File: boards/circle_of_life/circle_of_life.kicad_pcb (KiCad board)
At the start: 2 copper layers, 87.4 x 96.4 mm, 120 parts, among them IC1 ESP32-WROOM-32E-N8R2, IC2 TC1262-3.3VDB, IC3 TPS565242DRLR, IC4 LT3922EUFD#PBF, IC5 TXU0101DBVR, IC6 CP2102C-A01-GQFN28, J1 Water Pump Connector, J11 LED Connector, J2 Servo Motor Connector, J3 Power Connector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

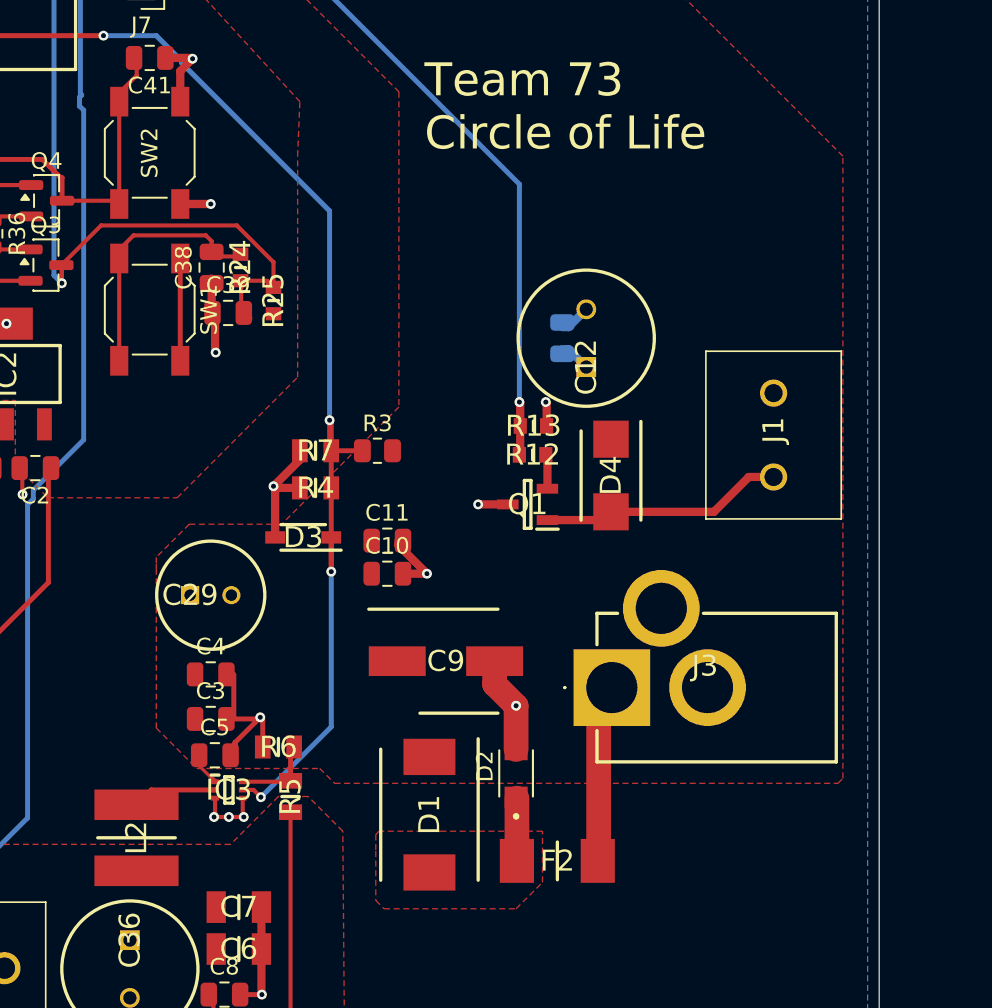
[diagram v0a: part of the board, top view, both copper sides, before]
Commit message: Fixed DRC for main board
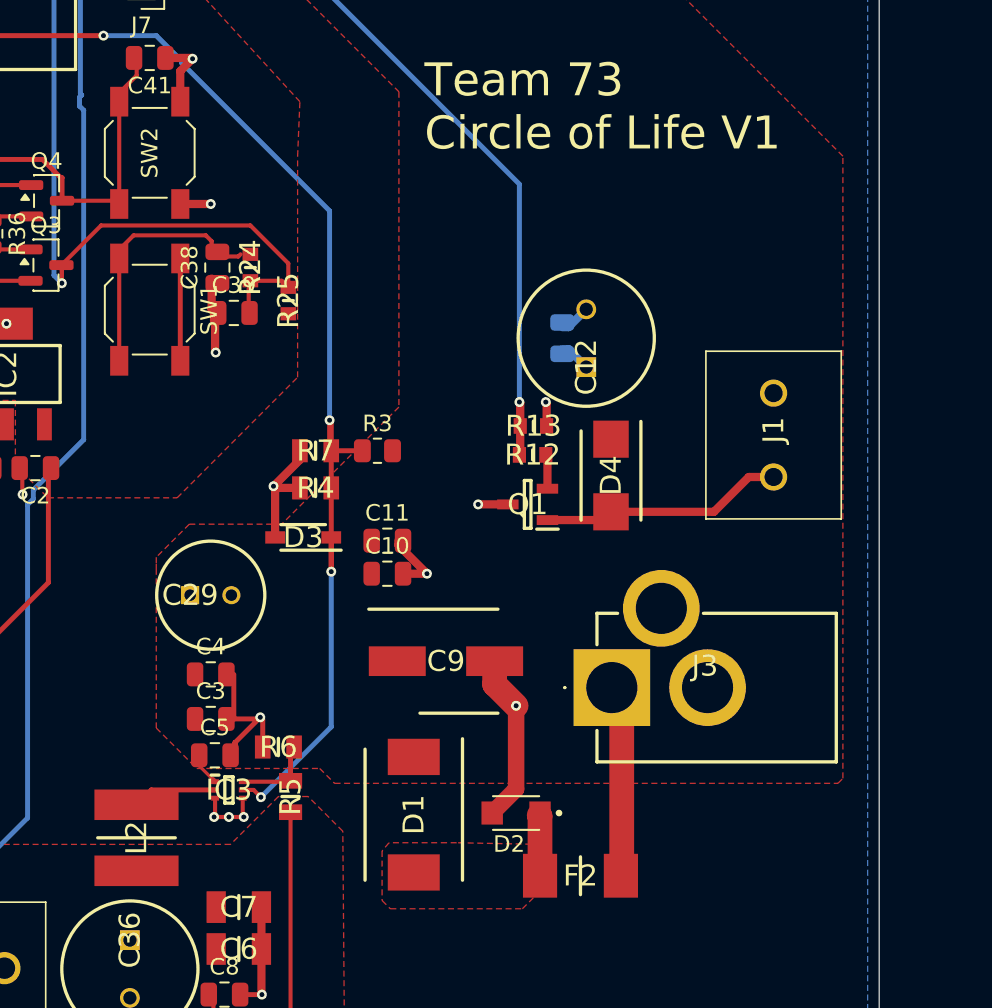
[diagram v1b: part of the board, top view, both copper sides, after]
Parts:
- moved D2 2.40 mm to (151.6, 184.8), turned to 180 degrees
- moved F2 1.66 mm to (155.5, 188.6)
- moved D1 0.95 mm to (145.4, 184.9)
- moved R25 0.90 mm to (137.8, 153.8)
- moved R24 0.60 mm to (135.5, 151.8)
- moved C38 0.35 mm to (133.5, 151.8)
- moved C39 0.35 mm to (134.5, 154.5)
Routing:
- net GND: track 150.0 -> 154.4 mm
- net Net-(D1-A): track 3.87 -> 2.78 mm
- net MCU_EN: track 60.9 -> 61.8 mm
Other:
- board text added: "Team 73 Circle of Life V1"
- board text removed: "Team 73 Circle of Life"
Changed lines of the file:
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@@
 	(footprint "SamacSys_Parts:RESC1608X55N"
 		(layer "F.Cu")
-		(at 134.902935 151.75 -90)
+		(at 135.5 151.75 -90)
 		(descr "RC0603")
 		(tags "Resistor")
@@
 	(footprint "SamacSys_Parts:RESC1608X55N"
 		(layer "F.Cu")
-		(at 136.902935 153.75 -90)
+		(at 137.8 153.75 -90)
 		(descr "RC0603")
 		(tags "Resistor")
@@
 	(footprint "Capacitor_SMD:C_0805_2012Metric"
 		(layer "F.Cu")
-		(at 133.152935 151.75 90)
+		(at 133.5 151.75 90)
 		(descr "Capacitor SMD 0805 (2012 Metric), square (rectangular) end terminal, IPC-7351 nominal, (Body size source: IPC-SM-782 page 76, https://www.pcb-3d.com/wordpress/wp-content/uploads/ipc-sm-782a_amendment_1_and_2.pdf, https://docs.google.com/spreadsheets/d/1BsfQQcO9C6DZCsRaXUlFlo91Tg2WpOkGARC1WS5S8t0/edit?usp=sharing), generated with kicad-footprint-generator")
 		(tags "capacitor")
@@
 	(footprint "Capacitor_SMD:C_0805_2012Metric"
 		(layer "F.Cu")
-		(at 134.152935 154.5)
+		(at 134.5 154.5)
 		(descr "Capacitor SMD 0805 (2012 Metric), square (rectangular) end terminal, IPC-7351 nominal, (Body size source: IPC-SM-782 page 76, https://www.pcb-3d.com/wordpress/wp-content/uploads/ipc-sm-782a_amendment_1_and_2.pdf, https://docs.google.com/spreadsheets/d/1BsfQQcO9C6DZCsRaXUlFlo91Tg2WpOkGARC1WS5S8t0/edit?usp=sharing), generated with kicad-footprint-generator")
 		(tags "capacitor")
@@
 	(footprint "SamacSys_Parts:TVS_SMF12A"
 		(layer "F.Cu")
-		(at 151.6 182.4 90)
+		(at 151.6 184.8 180)
 		(property "Reference" "D2"
-			(at 0.425 -1.885 90)
+			(at 0.425 -1.885 0)
 			(layer "F.SilkS")
 			(effects
@@
 		)
 		(property "Value" "SMF12A"
-			(at -0.25 -2.25 90)
+			(at -0.25 -2.25 0)
 			(layer "F.Fab")
 			(effects
@@
 		)
 		(property "Datasheet" "https://www.vishay.com/doc?85881"
-			(at 0 0 90)
+			(at 0 0 0)
 			(layer "F.Fab")
 			(hide yes)
@@
 		)
 		(property "Description" "200W unidirectional Transil Transient Voltage Suppressor, 12Vrwm, SMF"
-			(at 0 0 90)
+			(at 0 0 0)
 			(layer "F.Fab")
 			(hide yes)
@@
 		(attr smd)
 		(fp_line
-			(start -1.4 -1.02)
-			(end 1.4 -1.02)
+			(start 1.4 1.02)
+			(end -1.4 1.02)
 			(stroke
 				(width 0.127)
@@
 		)
 		(fp_line
-			(start 1.4 1.02)
-			(end -1.4 1.02)
+			(start -1.4 -1.02)
+			(end 1.4 -1.02)
 			(stroke
 				(width 0.127)
@@
 		)
 		(fp_line
-			(start 2.35 -1.125)
-			(end 2.35 1.125)
+			(start 2.35 1.125)
+			(end -2.35 1.125)
 			(stroke
 				(width 0.05)
@@
 		)
 		(fp_line
-			(start -2.35 -1.125)
-			(end 2.35 -1.125)
+			(start 2.35 -1.125)
+			(end 2.35 1.125)
 			(stroke
 				(width 0.05)
@@
 		)
 		(fp_line
-			(start 2.35 1.125)
-			(end -2.35 1.125)
+			(start -2.35 1.125)
+			(end -2.35 -1.125)
 			(stroke
 				(width 0.05)
@@
 		)
 		(fp_line
-			(start -2.35 1.125)
-			(end -2.35 -1.125)
+			(start -2.35 -1.125)
+			(end 2.35 -1.125)
 			(stroke
 				(width 0.05)
@@
 		)
 		(fp_line
-			(start 1.4 -0.875)
-			(end 1.4 0.875)
+			(start 1.4 0.875)
+			(end -1.4 0.875)
 			(stroke
 				(width 0.127)
@@
 		)
 		(fp_line
-			(start -1.4 -0.875)
-			(end 1.4 -0.875)
+			(start 1.4 -0.875)
+			(end 1.4 0.875)
 			(stroke
 				(width 0.127)
@@
 		)
 		(fp_line
-			(start 1.4 0.875)
-			(end -1.4 0.875)
+			(start -1.4 0.875)
+			(end -1.4 -0.875)
 			(stroke
 				(width 0.127)
@@
 		)
 		(fp_line
-			(start -1.4 0.875)
-			(end -1.4 -0.875)
+			(start -1.4 -0.875)
+			(end 1.4 -0.875)
 			(stroke
 				(width 0.127)
@@
 		)
 		(pad "1" smd rect
-			(at -1.45 0 90)
+			(at -1.45 0 180)
 			(size 1.3 1.4)
 			(layers "F.Cu" "F.Mask" "F.Paste")
@@
 		)
 		(pad "2" smd rect
-			(at 1.45 0 90)
+			(at 1.45 0 180)
 			(size 1.3 1.4)
 			(layers "F.Cu" "F.Mask" "F.Paste")
@@
 	(footprint "SamacSys_Parts:FUSC6125X236N"
 		(layer "F.Cu")
-		(at 154.1 187.7 180)
+		(at 155.5 188.6 180)
 		(descr "SF-2410FP1000W-2")
 		(tags "Fuse")
@@
 	(footprint "SamacSys_Parts:DIOM7959X262N"
 		(layer "F.Cu")
-		(at 146.35 184.9 -90)
+		(at 145.4 184.9 -90)
 		(descr "SK84LQ-TPsse")
 		(tags "Schottky Diode")
@@
 		(layer "Edge.Cuts")
 	)
-	(gr_text "Team 73\nCircle of Life"
+	(gr_text "Team 73\nCircle of Life V1"
 		(at 146.05 144.78 0)
 		(layer "F.SilkS")
@@
 	)
 	(segment
+		(start 151.6 183.35)
+		(end 150.15 184.8)
+		(width 1)
+		(layer "F.Cu")
+		(net 1)
+	)
+	(segment
 		(start 136.17 195.77)
 		(end 136.2 195.8)
@@
 	)
 	(segment
-		(start 151.6 178.3)
-		(end 151.6 180.95)
-		(width 1.5)
-		(layer "F.Cu")
-		(net 1)
-	)
-	(segment
 		(start 118.94 116.34)
 		(end 118.9 116.3)
@@
 	)
 	(segment
+		(start 151.6 178.3)
+		(end 151.6 183.35)
+		(width 1)
+		(layer "F.Cu")
+		(net 1)
+	)
+	(segment
 		(start 148.1 116.31)
 		(end 147.35 117.06)
@@
 	)
 	(segment
-		(start 136.502935 152.55)
-		(end 136.902935 152.95)
+		(start 124.077717 152.7)
+		(end 124.077717 151.577718)
 		(width 0.25)
 		(layer "F.Cu")
@@
 	)
 	(segment
+		(start 135.897065 152.55)
+		(end 135.4 153.047065)
+		(width 0.25)
+		(layer "F.Cu")
+		(net 15)
+	)
+	(segment
 		(start 124.077717 151.627282)
 		(end 124.077717 152.7)
@@
 	)
 	(segment
-		(start 124.077717 151.577718)
-		(end 126.455435 149.2)
+		(start 135.5 149.2)
+		(end 137.8 151.5)
 		(width 0.25)
 		(layer "F.Cu")
@@
 	)
 	(segment
-		(start 135.402935 154.926)
-		(end 135.502935 154.826)
+		(start 135.4 154.45)
+		(end 135.45 154.5)
 		(width 0.25)
 		(layer "F.Cu")
@@
 	)
 	(segment
-		(start 124.077717 152.7)
-		(end 124.077717 151.577718)
+		(start 135.4 153.047065)
+		(end 135.4 154.45)
 		(width 0.25)
 		(layer "F.Cu")
@@
 	)
 	(segment
-		(start 134.942935 152.59)
-		(end 134.902935 152.55)
+		(start 135.402935 154.926)
+		(end 135.502935 154.826)
 		(width 0.25)
 		(layer "F.Cu")
@@
 	)
 	(segment
-		(start 134.679935 149.2)
-		(end 136.902935 151.423)
+		(start 124.077717 151.577718)
+		(end 126.455435 149.2)
 		(width 0.25)
 		(layer "F.Cu")
@@
 	)
 	(segment
-		(start 134.942935 154.5)
-		(end 134.942935 152.59)
+		(start 137.4 152.55)
+		(end 135.897065 152.55)
 		(width 0.25)
 		(layer "F.Cu")
@@
 	)
 	(segment
-		(start 136.902935 151.423)
-		(end 136.902935 152.95)
+		(start 137.8 151.5)
+		(end 137.8 152.95)
 		(width 0.25)
 		(layer "F.Cu")
@@
 	)
 	(segment
-		(start 126.455435 149.2)
-		(end 134.679935 149.2)
+		(start 137.8 152.95)
+		(end 137.4 152.55)
 		(width 0.25)
 		(layer "F.Cu")
@@
 	)
 	(segment
-		(start 134.902935 152.55)
-		(end 136.502935 152.55)
+		(start 126.455435 149.2)
+		(end 135.5 149.2)
 		(width 0.25)
 		(layer "F.Cu")
@@
 	)
 	(segment
-		(start 151.65 183.9)
-		(end 151.6 183.85)
-		(width 1.2)
+		(start 153.05 184.9875)
+		(end 153 184.9375)
+		(width 1.5)
 		(layer "F.Cu")
 		(net 17)
 	)
 	(segment
-		(start 151.65 187.7)
-		(end 151.65 183.9)
+		(start 153.05 187.7)
+		(end 153.05 184.9875)
 		(width 1.5)
 		(layer "F.Cu")
@@
 	)
 	(segment
-		(start 156.6 178)
-		(end 156.6 187.65)
+		(start 158 178)
+		(end 158 187.65)
 		(width 1.5)
 		(layer "F.Cu")
@@
 	)
 	(segment
-		(start 156.6 187.65)
-		(end 156.55 187.7)
+		(start 158 187.65)
+		(end 157.95 187.7)
 		(width 0.25)
 		(layer "F.Cu")
@@
 		(polygon
 			(pts
-				(xy 143.1 187.1) (xy 143.1 190.1) (xy 143.6 190.6) (xy 151.6 190.6) (xy 153.2 189) (xy 153.2 185.9)
-				(xy 147.35 185.9) (xy 147.1 185.9) (xy 143.3 185.9) (xy 143.1 186.1)
+				(xy 143.479411 187.1) (xy 143.479411 190.1) (xy 143.979411 190.6) (xy 151.979411 190.6) (xy 153.579411 189)
+				(xy 153.1 186.7) (xy 148 186.6) (xy 147.4 186.6) (xy 144.5 186.6) (xy 143.9 186.6)
 			)
 		)
